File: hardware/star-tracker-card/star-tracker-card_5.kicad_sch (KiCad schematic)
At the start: 52 parts, among them Q1 MMBT2907, U10 TLVH431, U18 RCLAMP0504FB, U4 SN74LVC1G07DCK, U7 OSD3358-512M-BSM

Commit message: More EAGLE import cleanup
Fixed sheets, did some ERC cleanup, imported into layout, impmorted 4 layer DRC rules.
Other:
- note removed: "1.2"
- note removed: "OreSat Star Tracker: OSD Power/Misc"
- company: (none) -> Portland State Aerospace Society
- title: (none) -> OreSat Star Tracker
- moved on the sheet: C13, C14, C15, C18, C41, D1, JP101, JP104, Q1, R1, R15, R23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

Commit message: Schematic Overhaul of v1.3
Changed schematic to hierarchical, changed debug connector, updated OPD, removed JTAG, and ESD protection on removed connectors
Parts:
- removed C41: 0.1uF, star-tracker-card:.0603-A, symbol star-tracker-card-eagle-import:C-EU0603-A
- removed R73, R74, R75: 100, star-tracker-card:.0603-A, symbol star-tracker-card-eagle-import:R-US_0603-A
- removed TP112, TP151, TP155: TEST-POINT3X4, star-tracker-card:PAD.03X.04, symbol star-tracker-card-eagle-import:TEST-POINT3X4
- removed U18: RCLAMP0504FB, star-tracker-card:SC70-6, symbol star-tracker-card-eagle-import:RCLAMP0504FB
- added TP71, TP72, TP73: TEST-POINT3X4, oresat-misc:TestPoint_Pad_D1.0mm, symbol oresat-misc:Test-Point-1mm-round
- C13, C14, C15: footprint star-tracker-card:C1210 -> oresat-passives:0805-B-NOSILK; symbol star-tracker-card-eagle-import:C-EUC1210 -> Device:C_Small
- C18: footprint star-tracker-card:.0603-A -> oresat-passives:c_0603-SMALL; symbol star-tracker-card-eagle-import:C-EU0603-A -> Device:C_Small
- D1: symbol star-tracker-card-eagle-import:LED-GREEN0603 -> Device:LED
- R1, R15, R23, R28, R31: footprint star-tracker-card:.0603-A -> Resistor_SMD:R_0603_1608Metric; symbol star-tracker-card-eagle-import:R-US_0603-A -> Device:R_Small_US
- TP102, TP109, TP110, TP121, TP129, TP130, TP132, TP136, TP14, TP140, TP145, TP150, TP154, TP156, TP157, TP160, TP161, TP163, TP164, TP165, TP166, TP167, TP172, TP173, TP2, TP25, TP3, TP4: footprint star-tracker-card:PAD.03X.04 -> oresat-misc:TestPoint_Pad_D1.0mm; symbol star-tracker-card-eagle-import:TEST-POINT3X4 -> oresat-misc:Test-Point-1mm-round; now left out of the parts list
- U4: footprint star-tracker-card:C70(TI-DCK) -> Package_TO_SOT_SMD:SOT-353_SC-70-5; symbol star-tracker-card-eagle-import:SN74LVC1G07DCK -> oresat-ics:SN74LVC1G07DCK
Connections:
- net 3.3V: now also TP25.1; no longer TP25.P$1 (1)
- net 3.3VA: now also TP14.1, TP164.1; no longer TP14.P$1 (1), TP164.P$1 (1)
- net GND: now also D1.1 (K); no longer D1.C
- net PMIC_PGOOD: now also TP110.1; no longer TP110.P$1 (1)
- net VDD: now also TP3.1; no longer TP3.P$1 (1)
- net VIN_USB: now also TP2.1; no longer TP2.P$1 (1)
- net at R1.2: now also D1.2 (A); no longer D1.A
- net at JP101.1, U7.F8 (SYS_VDD3_3P3V@1), U7.F9 (VDDSHV4)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: now also TP165.1; no longer TP165.P$1 (1)
- net at U7.F13 (VDD_MPU): now also TP160.1; no longer TP160.P$1 (1)
- net at U7.N6 (PMIC_TS): now also TP129.1; no longer TP129.P$1 (1)
- net at U7.F11 (SYS_VDD2_3P3V@1), U7.G11 (SYS_VDD2_3P3V@2): now also TP161.1; no longer TP161.P$1 (1)
- net at U7.F10 (SYS_VDD_1P8V@1), U7.G10 (SYS_VDD_1P8V@2), U7.H10 (SYS_VDD_1P8V@3)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: now also TP163.1; no longer TP163.P$1 (1)
- net at U7.D5 (CAP_VDD_RTC): now also TP173.1; no longer TP173.P$1 (1)
- net at U7.G4 (VDD_CORE): now also TP154.1; no longer TP154.P$1 (1)
- net at U7.N7 (PMIC_BAT_SENSE), U7.P8 (VIN_BAT@1), U7.R8 (VIN_BAT@2)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: now also TP130.1, TP4.1; no longer TP130.P$1 (1), TP4.P$1 (1)
- net at U7.N10 (PMIC_POWER_EN), U7.N11 (PMIC_PWR_EN): now also TP121.1; no longer TP121.P$1 (1)
- net at U7.C10 (I2C0_SCL), U7.D10 (PMIC_SCL): now also TP71.1
- net at U7.C11 (I2C0_SDA), U7.D11 (PMIC_SDA): now also TP72.1
- net at U7.D4 (EXTINTN), U7.E4 (PMIC_NINT): now also TP167.1; no longer TP167.P$1 (1)
- net at U7.L4 (PMIC_NWAKEUP), U7.M4 (EXT_WAKEUP): now also TP140.1; no longer TP140.P$1 (1)
- net at U7.M13 (PMIC_NRESET): now also TP136.1; no longer TP136.P$1 (1)
- net at U7.M2 (EEPROM_WP): now also TP73.1
- net at U7.N4 (PMIC_LDO_PGOOD), U7.N5 (RTC_PWRONRSTN): now also TP132.1; no longer TP132.P$1 (1)
- net at U7.T11 (PMIC_PB_IN): now also TP102.1; no longer TP102.P$1 (1)
- net at U7.G13 (VDDS_PLL): now also TP166.1; no longer TP166.P$1 (1)
- net at U7.J6 (NC@2): now also TP150.1; no longer TP150.P$1 (1)
- net at U7.D12 (NC@1): now also TP172.1; no longer TP172.P$1 (1)
- net at U7.F4 (VDDS_DDR): now also TP156.1; no longer TP156.P$1 (1)
- net at U7.H6 (VPP): now also TP157.1; no longer TP157.P$1 (1)
- net at U7.K4 (NC@3): now also TP145.1; no longer TP145.P$1 (1)
- net RESET#: no longer names the net of U4.4 (Y), U7.R11 (WARMRSTN)
- net RESET#: now also TP109.1; no longer TP109.P$1 (1)
- no-connect marks 1 -> 0
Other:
- note removed: "ESD protection clamping diodes for I2C0 lines. This is required because these lines are routed externally so the internal EEPROM can be programmed."

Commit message: Updated Octavo schematic
Removed many testpoints, added filter to 1.8v reference, tied some signals to ground with pull down resistor, added NCs to multiple pins.
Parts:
- removed TP130, TP145, TP150, TP157, TP165, TP172, TP173, TP2: TEST-POINT3X4, oresat-misc:TestPoint_Pad_D1.0mm, symbol oresat-misc:Test-Point-1mm-round
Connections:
- no-connect marks 0 -> 5
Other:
- note removed: "" ""
- moved on the sheet: TP110, TP129, TP154, TP156, TP160, TP161, TP166, TP4, U7E, U7F

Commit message: Update
Update to the octavo schematic
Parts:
- removed JP101, JP104: JUMPER-SMT_2_NC_TRACE_SILK, star-tracker-card:SMT-JUMPER_2_NC_TRACE_SILK, symbol star-tracker-card-eagle-import:JUMPER-SMT_2_NC_TRACE_SILK
- removed TP14, TP154, TP156, TP160, TP166, TP71, TP72, TP73: TEST-POINT3X4, oresat-misc:TestPoint_Pad_D1.0mm, symbol oresat-misc:Test-Point-1mm-round
- removed unit 6 of U7
- removed unit 5 of U7
- added C47, C65: 100n, oresat-passives:0603-C-NOSILK, symbol Device:C_Small
- added C93: 22u, Capacitor_SMD:C_1210_3225Metric, symbol Device:C_Small
- added R78: 10k, oresat-passives:0603-C-NOSILK, symbol Device:R_Small_US
- Q1: symbol star-tracker-card-eagle-import:MMBT2907SMD -> Transistor_BJT:Q_PNP_BEC
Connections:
- net 3.3VA is gone; now on an unnamed net: C18.1, TP164.1, U4.5 (VCC), U7.K11 (SYS_RTC_1P8V@1), U7.L11 (SYS_RTC_1P8V@2)
- net 3.3V: now also R78.2
- net 5V: now also C65.1, C93.1
- net GND: now also C47.2, C65.2, C93.2
- net at R23.1, U10.2 (CATHODE): now also Q1.1 (B); no longer Q1.B
- net at R23.2, R28.2: now also Q1.2 (E), U7.F8 (SYS_VDD3_3P3V@1), U7.F9 (VDDSHV4), U7.G8 (SYS_VDD3_3P3V@2), U7.G9 (VDDSHV5), U7.H7 (SYS_VDD3_3P3V@3), U7.H8 (SYS_VDD3_3P3V@4), U7.H9 (VDDSHV6), U7.J7 (SYS_VDD3_3P3V@5), U7.J8 (SYS_VDD3_3P3V@6), U7.J9 (VDDSHV1), U7.K8 (SYS_VDD3_3P3V@7), U7.K9 (VDDSHV2), U7.L8 (SYS_VDD3_3P3V@8), U7.L9 (VDDSHV3); no longer Q1.E
- net PMIC_SCL: now reaches U7.C10 (I2C0_SCL), U7.D10 (PMIC_SCL)
- net at R31.1, U10.3 (ANODE): now also Q1.3 (C); no longer Q1.C
- net nRESET: now reaches TP109.1, U4.4 (Y), U7.R11 (WARMRSTN)
- net nRESET: now also C47.1, R78.1
- net PMIC_SDA: now reaches U7.C11 (I2C0_SDA), U7.D11 (PMIC_SDA)
- net EEPROM_WP: now reaches U7.M2 (EEPROM_WP)
- no-connect marks 5 -> 0
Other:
- moved on the sheet: C14, C18, D1, R1, TP129, TP163, TP4

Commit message: DRC hunting
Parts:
- D1: footprint star-tracker-card:LED-0603 -> LED_SMD:LED_0603_1608Metric
- Q1: footprint star-tracker-card:SOT23-BEC -> Package_TO_SOT_SMD:SOT-23-3
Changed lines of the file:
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@@
 			)
 		)
-		(property "Footprint" "star-tracker-card:LED-0603"
+		(property "Footprint" "LED_SMD:LED_0603_1608Metric"
 			(at 215.9 90.17 0)
 			(effects
@@
 			)
 		)
-		(property "Footprint" "star-tracker-card:SOT23-BEC"
+		(property "Footprint" "Package_TO_SOT_SMD:SOT-23-3"
 			(at 212.09 128.27 0)
 			(effects

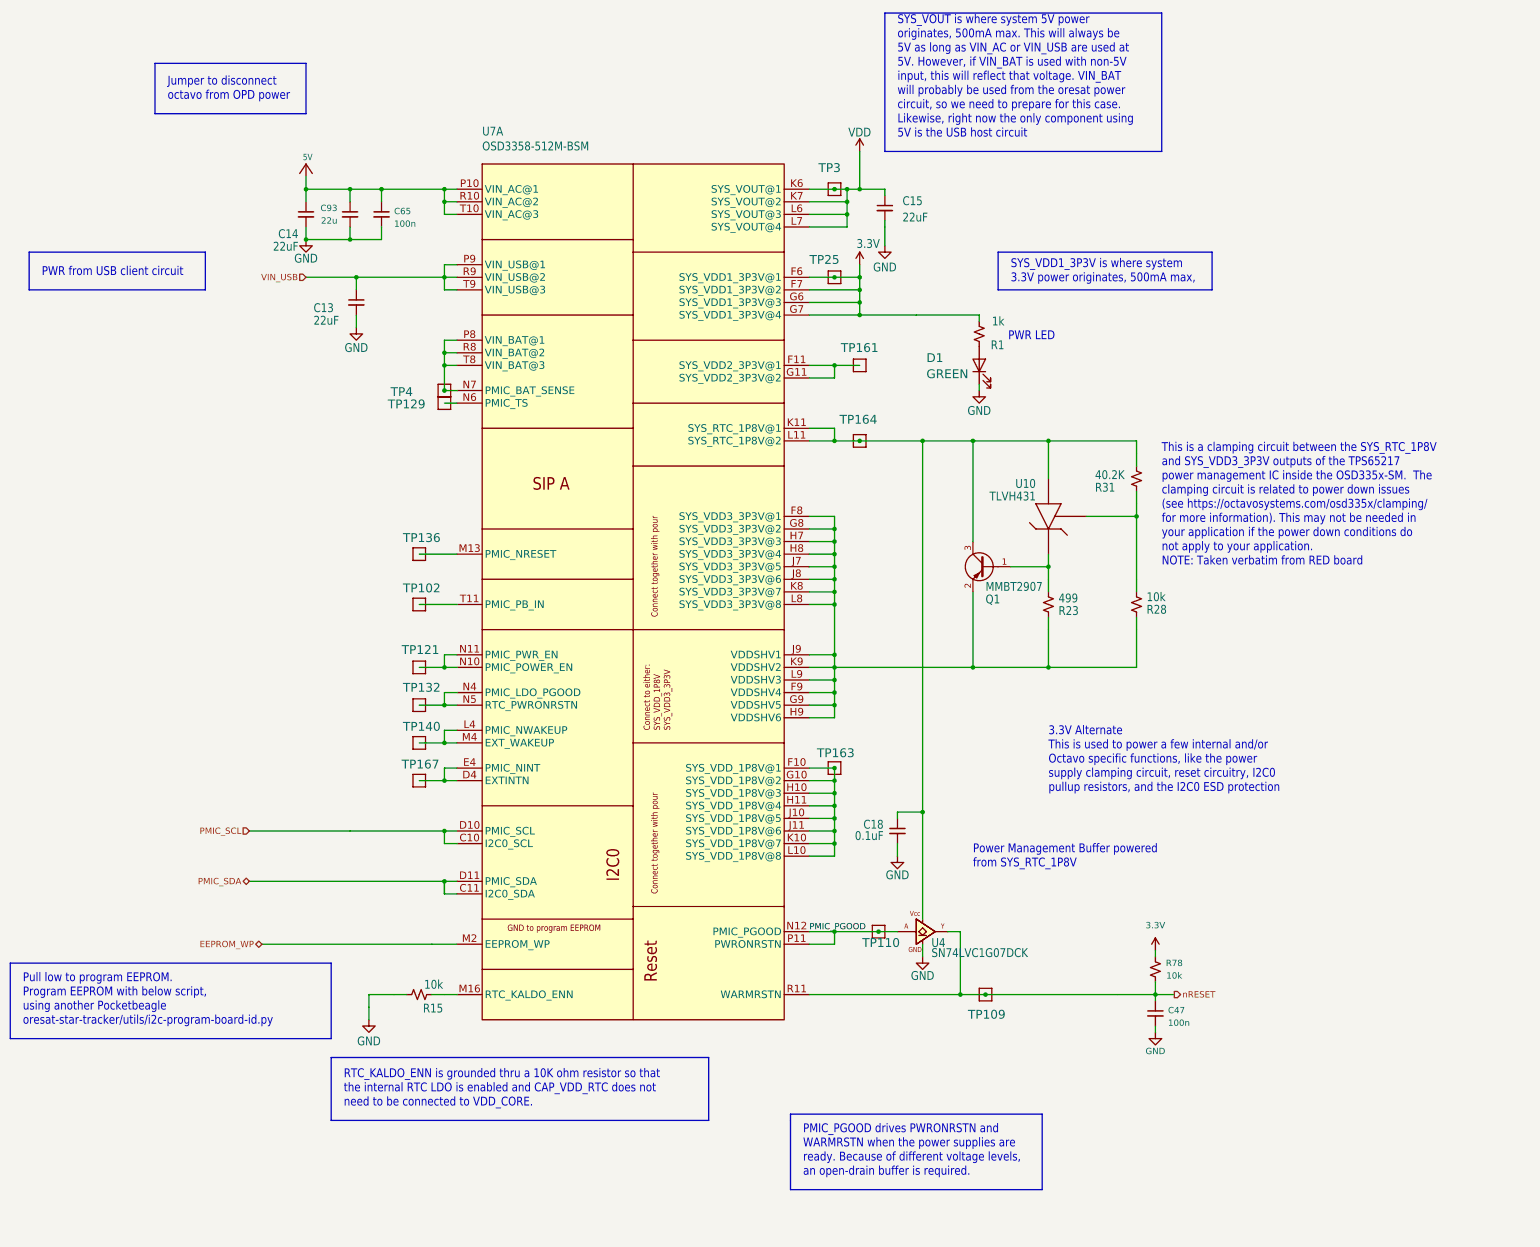
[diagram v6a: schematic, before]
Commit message: Big almost-done cleanup
Fixed a bunch of things in the schematic. Compared against C3 Octavo. Fixed all weird ERCs. Cleaned up a lot of planes on the layout. Moved uart switch, rerouted a bunch of traces for better layout. Fixed library issues, and board/sch sync issues.
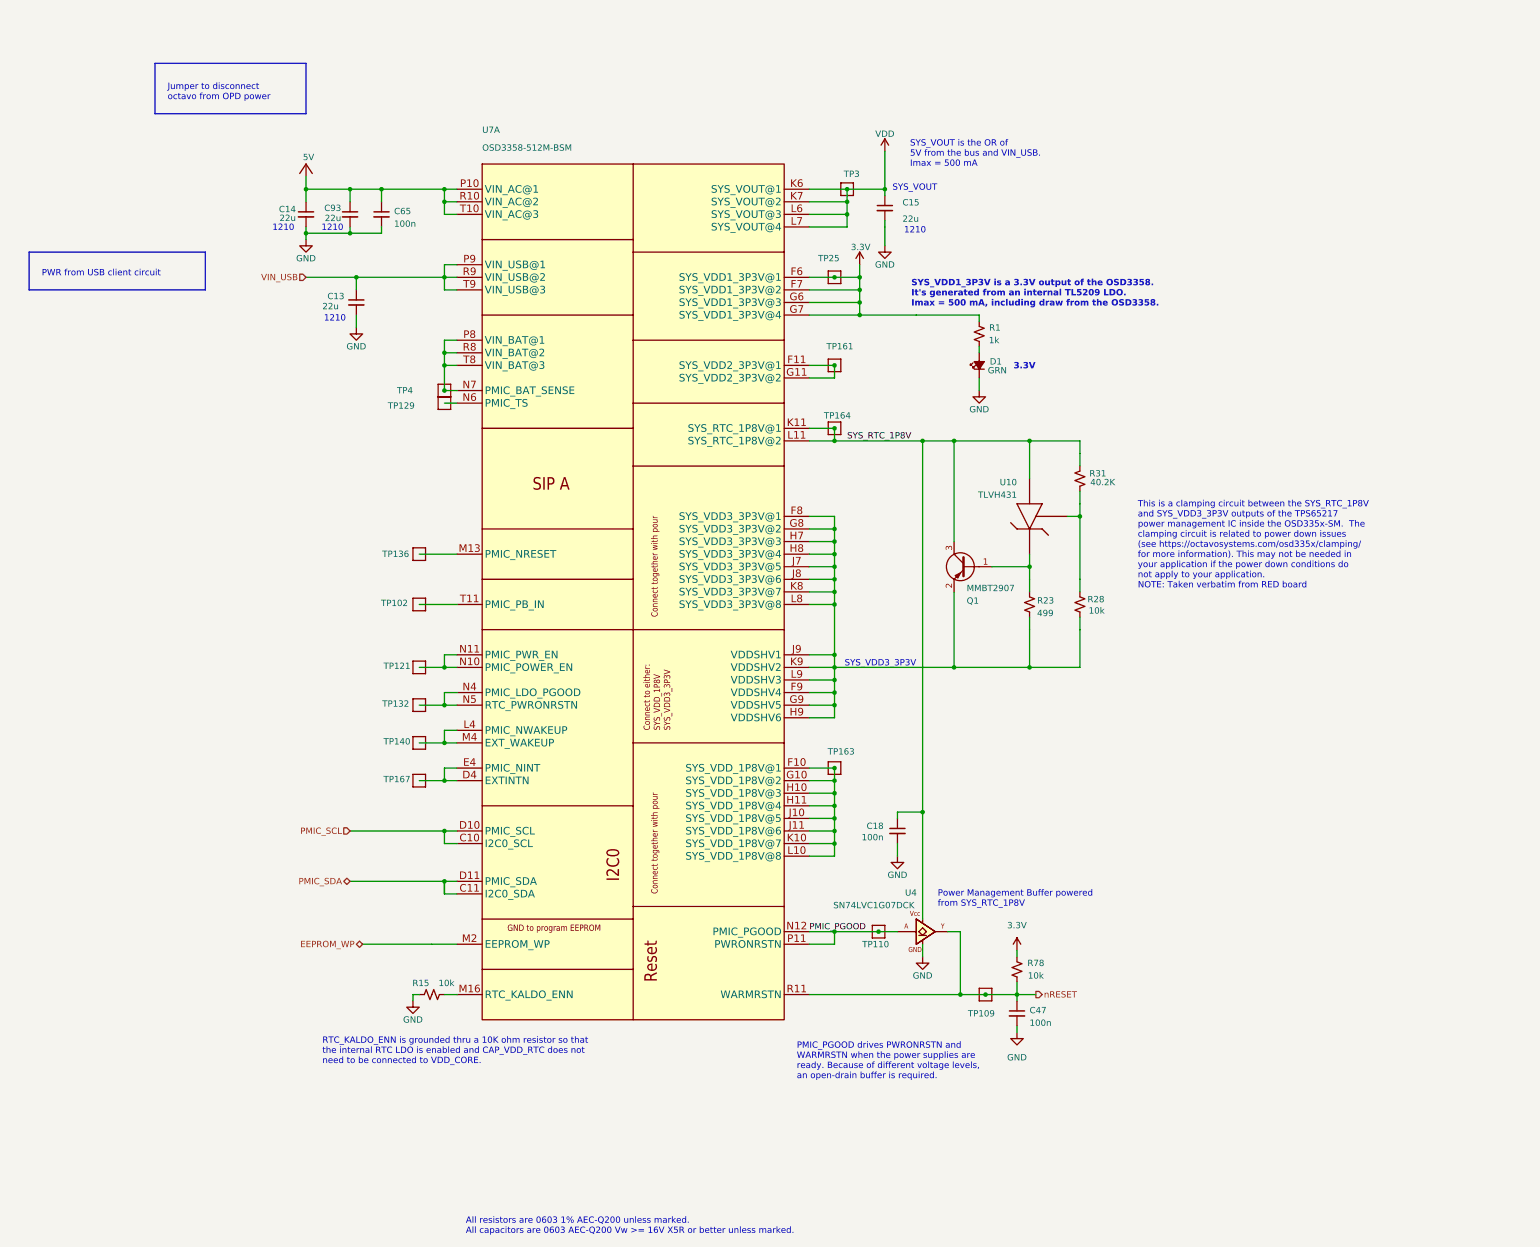
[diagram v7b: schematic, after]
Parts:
- C13, C14, C15: value 22uF -> 22u; footprint oresat-passives:0805-B-NOSILK -> Capacitor_SMD:C_1210_3225Metric
- C18: value 0.1uF -> 100n; footprint oresat-passives:c_0603-SMALL -> oresat-passives:0603-C-NOSILK
- C47, C65, C93, R78: DST DigiKey -> (none)
- D1: value GREEN -> GRN; symbol Device:LED -> Device:LED_Small_Filled
- R1, R15, R23, R28, R31: footprint Resistor_SMD:R_0603_1608Metric -> oresat-passives:0603-C-NOSILK
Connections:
- net SYS_RTC_1P8V: now reaches C18.1, Q1.3 (C), R31.1, TP164.1, U10.3 (ANODE), U4.5 (VCC), U7.K11 (SYS_RTC_1P8V@1), U7.L11 (SYS_RTC_1P8V@2)
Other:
- note added: "1210"
- note added: "3.3V"
- note added: "All resistors are 0603 1% AEC-Q200 unless marked. All capacitors are 0603 AEC-Q200 Vw >= 16V X5R or better unless marked."
- note added: "SYS_VDD1_3P3V is a 3.3V output of the OSD3358. It's generated from an internal TL5209 LDO. Imax = 500 mA, including draw from the OSD3358."
- note added: "SYS_VDD3_3P3V"
- note added: "SYS_VOUT"
- note added: "SYS_VOUT is the OR of 5V from the bus and VIN_USB. Imax = 500 mA"
- note removed: "3.3V Alternate This is used to power a few internal and/or Octavo specific functions, like the power supply clamping circuit, reset circuitry, I2C0 pullup resistors, and the I2C0 ESD protection"
- note removed: "PWR LED"
- note removed: "Pull low to program EEPROM. Program EEPROM with below script, using another Pocketbeagle oresat-star-tracker/utils/i2c-program-board-id.py"
- note removed: "SYS_VDD1_3P3V is where system 3.3V power originates, 500mA max,"
- note removed: "SYS_VOUT is where system 5V power originates, 500mA max. This will always be 5V as long as VIN_AC or VIN_USB are used at 5V. However, if VIN_BAT is used with non-5V input, this will reflect that voltage. VIN_BAT will probably be used from the oresat power circuit, so we need to prepare for this case. Likewise, right now the only component using 5V is the USB host circuit"
- moved on the sheet: C47, Q1, R15, R23, R28, R31, R78, TP161, TP164, TP3, U10

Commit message: BOM 99% completed, push for final review
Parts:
- C13, C14, C15: DIS (none) -> DigiKey; DPN (none) -> 587-5949-1-ND; MFR (none) -> Taiyo Yuden; MPN (none) -> TMK325B7226KMHP
- C18: DIS (none) -> DigiKey; DPN (none) -> 399-6856-1-ND; MFR (none) -> KEMET; MPN (none) -> C0603C104K5RACAUTO
- C47, C65, C93, R78: DIS (none) -> DigiKey
- D1: DIS (none) -> DigiKey; DPN (none) -> 732-4971-1-ND; MFR (none) -> Wurth; MPN (none) -> 150060GS75000
- Q1: DIS (none) -> DigiKey; DPN (none) -> 5399-MMBT2907CT-ND; MFR (none) -> Shenzhen Slkormicro Semicon Co., Ltd.; MPN (none) -> MMBT2907
- R1: DIS (none) -> DigiKey; DPN (none) -> RMCF0603FT2K70CT-ND; MFR (none) -> Stackpole Electronics; MPN (none) -> RMCF0603FT1K00
- R15, R28: DIS (none) -> DigiKey; DPN (none) -> RMCF0603FT10K0CT-ND; MFR (none) -> Stackpole Electronics; MPN (none) -> RMCF0603FT10K0
- R23: DIS (none) -> DigiKey; DPN (none) -> RMCF0603FT499RCT-ND; MFR (none) -> Stackpole Electronics Inc; MPN (none) -> RMCF0603FT499R
- R31: DIS (none) -> DigiKey; DPN (none) -> RMCF0603FT40K2CT-ND; MFR (none) -> Stackpole Electronics Inc; MPN (none) -> RMCF0603FT40K2
- U10: DIS (none) -> DigiKey; DPN (none) -> 296-32429-1-ND; MFR (none) -> Texas Instruments; MPN (none) -> TLVH431BCDBZT
- U4: DIS (none) -> DigiKey; DPN (none) -> 296-12464-1-ND; MFR (none) -> Texas Instruments; MPN (none) -> SN74AUC1G07DCKR
- U7: DIS (none) -> DigiKey; DPN (none) -> 1676-OSD3358-1G-ISM-ND; MFR (none) -> Octavo Systems LLC; MPN (none) -> OSD3358-1G-ISM
